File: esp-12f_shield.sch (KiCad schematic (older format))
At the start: 57 parts, among them J1 UART, J10 Conn_01x01, J11 Conn_01x01, J12 Conn_01x01, J13 Conn_01x01, J2 SPI, J3 Sold_Pad_small, J4 Start, J5 Conn_01x01, J6 Conn_01x01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

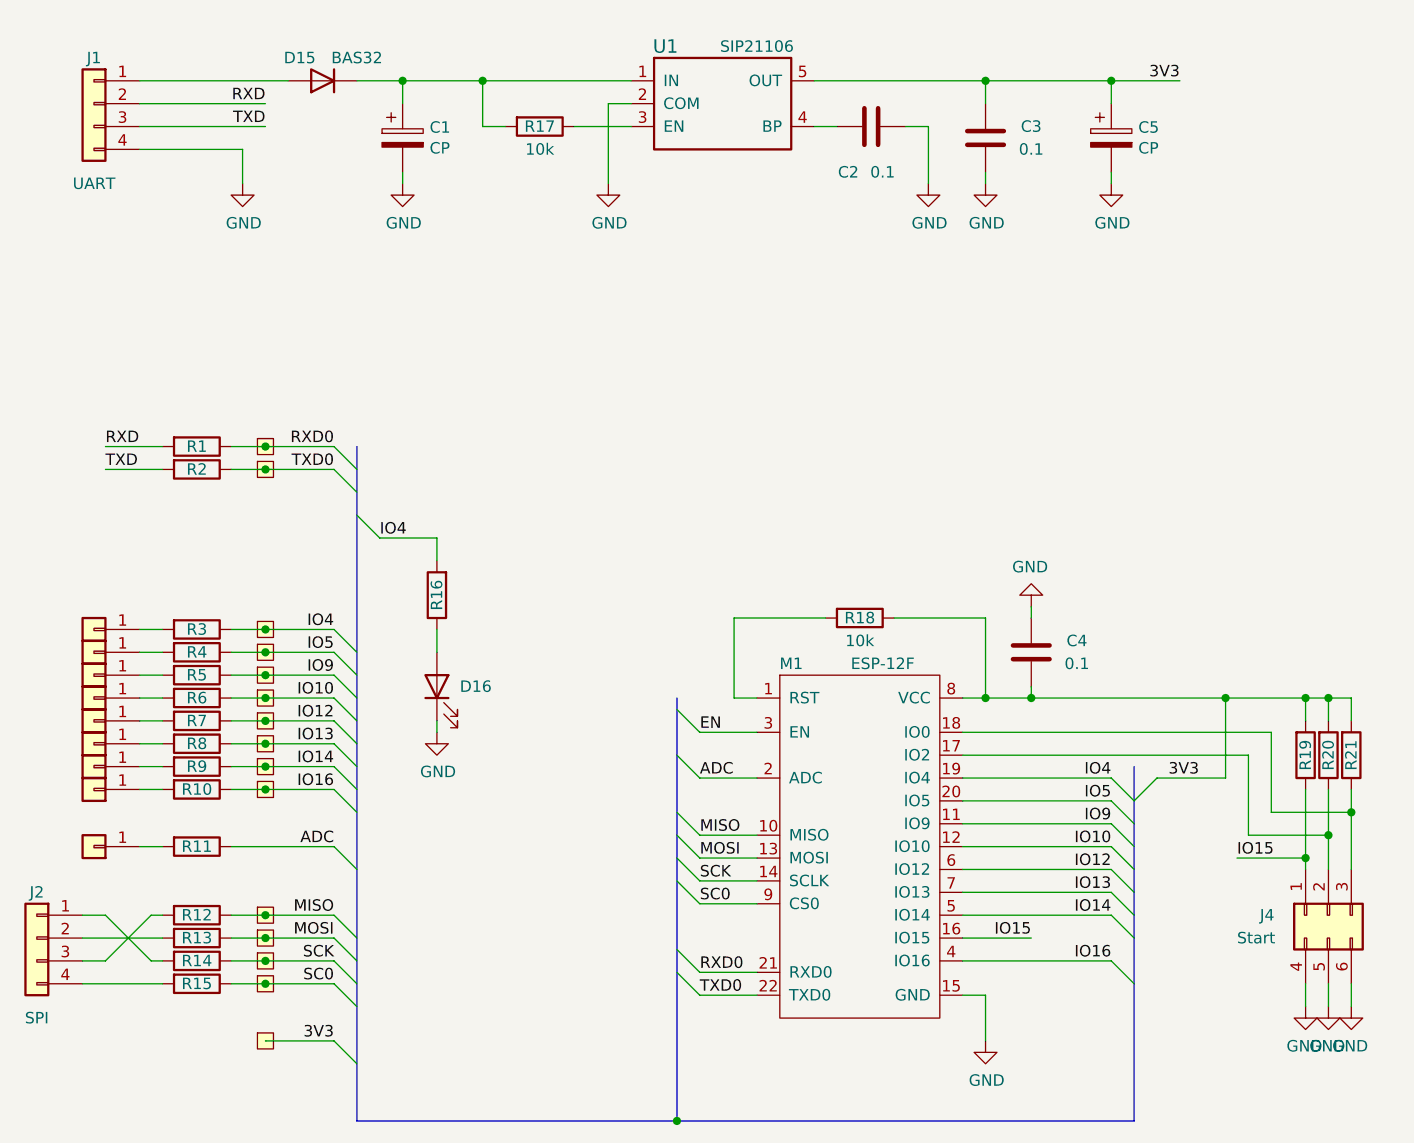
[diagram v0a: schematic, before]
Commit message: paruosta schema ir plokste
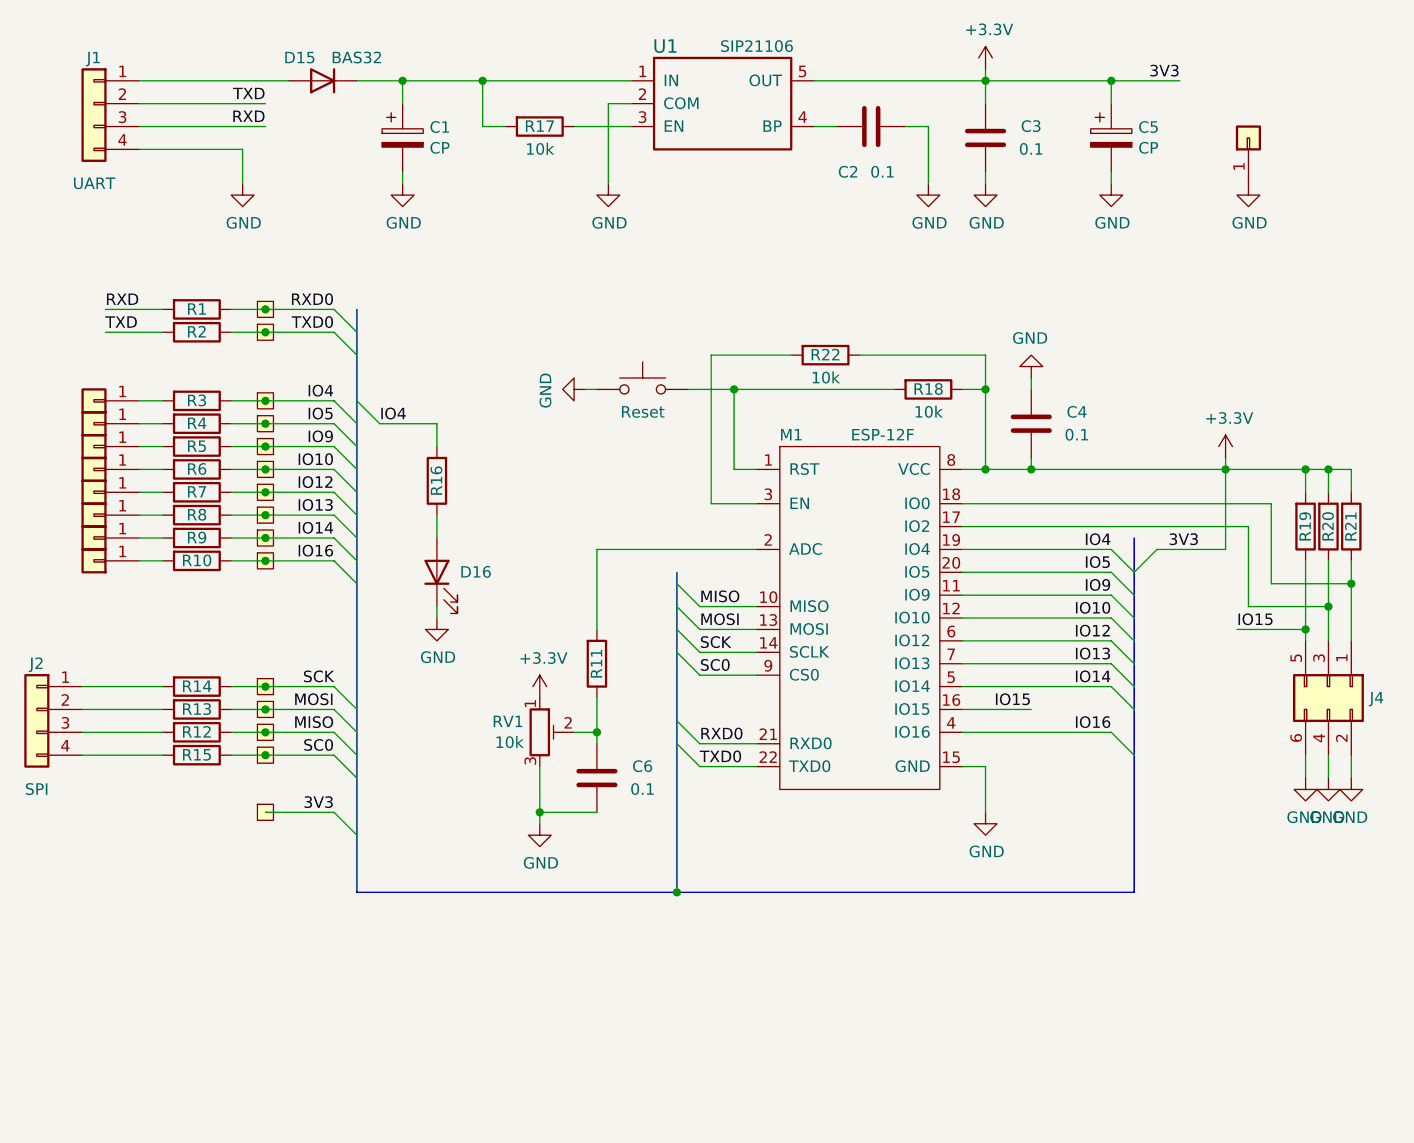
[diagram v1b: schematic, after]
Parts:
- removed J4: Start, symbol Connector_Generic:Conn_02x03_Top_Bottom
- added C6: 0.1, Capacitor_SMD:C_0805_2012Metric, symbol Device:C
- added J4: Conn_02x03_Odd_Even, Connector_PinHeader_2.54mm:PinHeader_2x03_P2.54mm_Vertical, symbol Connector_Generic:Conn_02x03_Odd_Even
- added R22: 10k, Resistor_SMD:R_0805_2012Metric_Pad1.15x1.40mm_HandSolder, symbol Device:R
- added RV1: 10k, Potentiometer_THT:Potentiometer_Bourns_3296Y_Vertical, symbol Device:R_POT_TRIM
- added SW1: Reset, Button_Switch_THT:SW_DIP_SPSTx01_Slide_6.7x4.1mm_W7.62mm_P2.54mm_LowProfile, symbol Switch:SW_Push
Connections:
- net GND: now also J13.1 (Pin_1), C6.1, J4.2 (Pin_2), J4.4 (Pin_4), J4.6 (Pin_6), RV1.3, SW1.1
- net IO15: now also J4.5 (Pin_5)
- net RXD: now also J1.3 (Pin_3); no longer J1.2 (Pin_2)
- net TXD: now also J1.2 (Pin_2); no longer J1.3 (Pin_3)
- net at M1.1 (RST), R18.2: now also SW1.2
- net at M1.17 (IO2), R20.1: now also J4.3 (Pin_3)
- net at M1.18 (IO0), R21.1: now also J4.1 (Pin_1)
- net at R11.2: now also M1.2 (ADC); no longer J13.1 (Pin_1)
- net 3V3 renamed +3V3
- net +3V3: now also R22.1, RV1.1
- net ADC: no longer names the net of R11.1
- net ADC: now also C6.2, RV1.2; no longer M1.2 (ADC)
- net EN: no longer names the net of M1.3 (EN)
- net EN: now also R22.2
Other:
- moved on the sheet: C4, D16, J2, M1, R1, R10, R11, R12, R13, R14, R15, R16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
